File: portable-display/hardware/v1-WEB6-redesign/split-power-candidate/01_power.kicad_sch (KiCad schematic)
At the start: 34 parts, among them J1 USB4105-GF-A-060, J2 1S LiPo + NTC, SW5 POWER, U1 AXP2101, U9 USBLC6-2SC6

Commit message: chore(bom): assign LCSC/MPN to 62 parts (JLC basic preferred)
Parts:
- C1, C2: LCSC (none) -> C86295; MPN 0603 22u X5R -> CL10A226MP8NUNE
- C10: LCSC (none) -> C23630; MPN 0603 2.2u X5R -> CL10A225KO8NNNC
- C11, C3, C33: LCSC (none) -> C15849; MPN 0603 1u X5R -> CL10A105KB8NNNC
- C32: LCSC (none) -> C19702; MPN 0603 10u X5R -> CL10A106KP8NNNC
- C38: LCSC (none) -> C23630; MPN (none) -> CL10A225KO8NNNC
- C39: LCSC (none) -> C1525; MPN (none) -> CL05B104KO5NNNC
- C4, C5, C6, C7, C8, C9: LCSC (none) -> C59461; MPN 0603 22u X5R -> CL10A226MQ8NRNC
- C40, C41: LCSC (none) -> C15849; MPN (none) -> CL10A105KB8NNNC
- D1: LCSC (none) -> C12624; MPN 0603 Green LED -> KT-0603G
- L1, L2, L3: LCSC (none) -> C97002; MPN 1uH 2A shielded -> WPN201610H1R0MT
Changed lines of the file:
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@@
 			)
 		)
-		(property "MPN" "0603 1u X5R"
+		(property "MPN" "CL10A105KB8NNNC"
 			(at 459.740 76.200 0)
 			(effects
@@
 			)
 		)
-		(property "LCSC" ""
+		(property "LCSC" "C15849"
 			(at 459.740 76.200 0)
 			(effects
@@
 			)
 		)
-		(property "MPN" "0603 22u X5R"
+		(property "MPN" "CL10A226MQ8NRNC"
 			(at 195.580 91.440 0)
 			(effects
@@
 			)
 		)
-		(property "LCSC" ""
+		(property "LCSC" "C59461"
 			(at 195.580 91.440 0)
 			(effects
@@
 			)
 		)
-		(property "MPN" "0603 22u X5R"
+		(property "MPN" "CL10A226MQ8NRNC"
 			(at 327.660 105.410 0)
 			(effects
@@
 			)
 		)
-		(property "LCSC" ""
+		(property "LCSC" "C59461"
 			(at 327.660 105.410 0)
 			(effects
@@
 			)
 		)
-		(property "MPN" ""
+		(property "MPN" "CL10A105KB8NNNC"
 			(at 459.740 105.410 0)
 			(effects
@@
 			)
 		)
-		(property "LCSC" ""
+		(property "LCSC" "C15849"
 			(at 459.740 105.410 0)
 			(effects
@@
 			)
 		)
-		(property "MPN" "0603 22u X5R"
+		(property "MPN" "CL10A226MQ8NRNC"
 			(at 63.500 119.380 0)
 			(effects
@@
 			)
 		)
-		(property "LCSC" ""
+		(property "LCSC" "C59461"
 			(at 63.500 119.380 0)
 			(effects
@@
 			)
 		)
-		(property "MPN" "0603 22u X5R"
+		(property "MPN" "CL10A226MP8NUNE"
 			(at 195.580 120.650 0)
 			(effects
@@
 			)
 		)
-		(property "LCSC" ""
+		(property "LCSC" "C86295"
 			(at 195.580 120.650 0)
 			(effects
@@
 			)
 		)
-		(property "MPN" ""
+		(property "MPN" "CL10A105KB8NNNC"
 			(at 63.500 148.590 0)
 			(effects
@@
 			)
 		)
-		(property "LCSC" ""
+		(property "LCSC" "C15849"
 			(at 63.500 148.590 0)
 			(effects
@@
 			)
 		)
-		(property "MPN" "0603 22u X5R"
+		(property "MPN" "CL10A226MQ8NRNC"
 			(at 195.580 149.860 0)
 			(effects
@@
 			)
 		)
-		(property "LCSC" ""
+		(property "LCSC" "C59461"
 			(at 195.580 149.860 0)
 			(effects
@@
 			)
 		)
-		(property "MPN" "0603 22u X5R"
+		(property "MPN" "CL10A226MQ8NRNC"
 			(at 327.660 163.830 0)
 			(effects
@@
 			)
 		)
-		(property "LCSC" ""
+		(property "LCSC" "C59461"
 			(at 327.660 163.830 0)
 			(effects
@@
 			)
 		)
-		(property "MPN" "1uH 2A shielded"
+		(property "MPN" "WPN201610H1R0MT"
 			(at 459.740 163.830 0)
 			(effects
@@
 			)
 		)
-		(property "LCSC" ""
+		(property "LCSC" "C97002"
 			(at 459.740 163.830 0)
 			(effects
@@
 			)
 		)
-		(property "MPN" "0603 1u X5R"
+		(property "MPN" "CL10A105KB8NNNC"
 			(at 63.500 177.800 0)
 			(effects
@@
 			)
 		)
-		(property "LCSC" ""
+		(property "LCSC" "C15849"
 			(at 63.500 177.800 0)
 			(effects
@@
 			)
 		)
-		(property "MPN" "1uH 2A shielded"
+		(property "MPN" "WPN201610H1R0MT"
 			(at 195.580 179.070 0)
 			(effects
@@
 			)
 		)
-		(property "LCSC" ""
+		(property "LCSC" "C97002"
 			(at 195.580 179.070 0)
 			(effects
@@
 			)
 		)
-		(property "MPN" "0603 22u X5R"
+		(property "MPN" "CL10A226MP8NUNE"
 			(at 327.660 193.040 0)
 			(effects
@@
 			)
 		)
-		(property "LCSC" ""
+		(property "LCSC" "C86295"
 			(at 327.660 193.040 0)
 			(effects
@@
 			)
 		)
-		(property "MPN" "1uH 2A shielded"
+		(property "MPN" "WPN201610H1R0MT"
 			(at 195.580 208.280 0)
 			(effects
@@
 			)
 		)
-		(property "LCSC" ""
+		(property "LCSC" "C97002"
 			(at 195.580 208.280 0)
 			(effects
@@
 			)
 		)
-		(property "MPN" "0603 Green LED"
+		(property "MPN" "KT-0603G"
 			(at 459.740 222.250 0)
 			(effects
@@
 			)
 		)
-		(property "LCSC" ""
+		(property "LCSC" "C12624"
 			(at 459.740 222.250 0)
 			(effects
@@
 			)
 		)
-		(property "MPN" "0603 1u X5R"
+		(property "MPN" "CL10A105KB8NNNC"
 			(at 195.580 237.490 0)
 			(effects
@@
 			)
 		)
-		(property "LCSC" ""
+		(property "LCSC" "C15849"
 			(at 195.580 237.490 0)
 			(effects
@@
 			)
 		)
-		(property "MPN" ""
+		(property "MPN" "CL05B104KO5NNNC"
 			(at 327.660 251.460 0)
 			(effects
@@
 			)
 		)
-		(property "LCSC" ""
+		(property "LCSC" "C1525"
 			(at 327.660 251.460 0)
 			(effects
@@
 			)
 		)
-		(property "MPN" "0603 2.2u X5R"
+		(property "MPN" "CL10A225KO8NNNC"
 			(at 63.500 265.430 0)
 			(effects
@@
 			)
 		)
-		(property "LCSC" ""
+		(property "LCSC" "C23630"
 			(at 63.500 265.430 0)
 			(effects
@@
 			)
 		)
-		(property "MPN" "0603 22u X5R"
+		(property "MPN" "CL10A226MQ8NRNC"
 			(at 195.580 266.700 0)
 			(effects
@@
 			)
 		)
-		(property "LCSC" ""
+		(property "LCSC" "C59461"
 			(at 195.580 266.700 0)
 			(effects
@@
 			)
 		)
-		(property "MPN" ""
+		(property "MPN" "CL10A225KO8NNNC"
 			(at 327.660 280.670 0)
 			(effects
@@
 			)
 		)
-		(property "LCSC" ""
+		(property "LCSC" "C23630"
 			(at 327.660 280.670 0)
 			(effects
@@
 			)
 		)
-		(property "MPN" "0603 10u X5R"
+		(property "MPN" "CL10A106KP8NNNC"
 			(at 459.740 280.670 0)
 			(effects
@@
 			)
 		)
-		(property "LCSC" ""
+		(property "LCSC" "C19702"
 			(at 459.740 280.670 0)
 			(effects

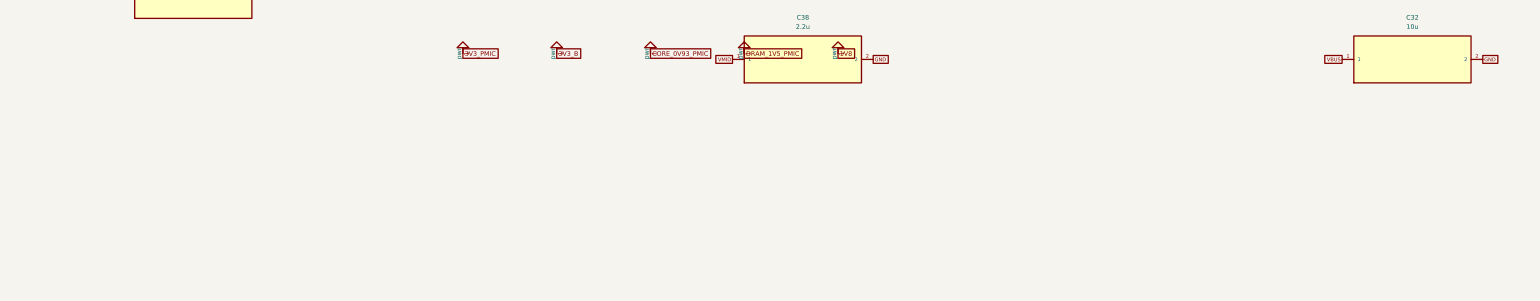
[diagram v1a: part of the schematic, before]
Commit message: `feat(pcb): improve V1 decoupling, test access, and routing`
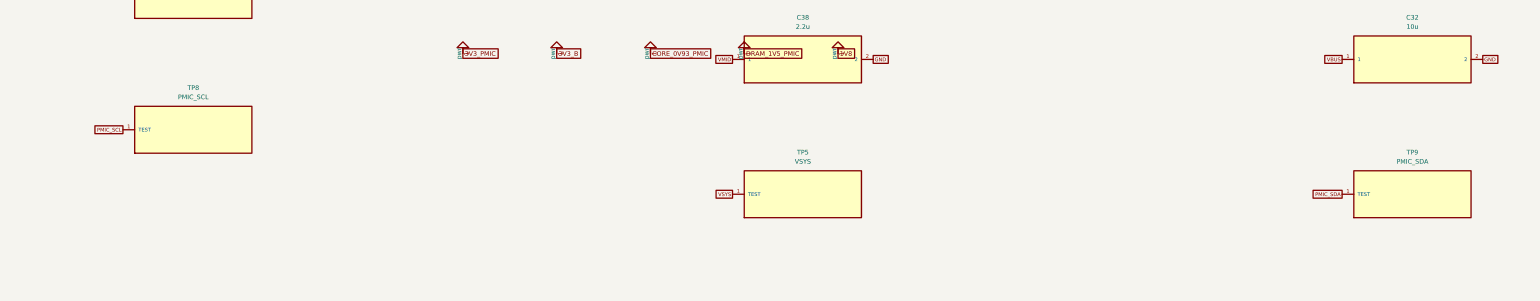
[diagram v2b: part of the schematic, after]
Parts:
- added TP5: VSYS, Sameat:TestPoint_Pad_D1.0mm, symbol Sameat:TP5_VSYS
- added TP8: PMIC_SCL, Sameat:TestPoint_Pad_D1.0mm, symbol Sameat:TP8_PMIC_SCL
- added TP9: PMIC_SDA, Sameat:TestPoint_Pad_D1.0mm, symbol Sameat:TP9_PMIC_SDA
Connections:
- net PMIC_SCL: now also TP8.1 (TEST)
- net PMIC_SDA: now also TP9.1 (TEST)
- net VSYS: now also TP5.1 (TEST)
